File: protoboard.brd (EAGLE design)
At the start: 99.1 x 48.3 mm, 118 parts, among them J3 AVX_6-PIN_009159006061916, J4 CORTEX_DEBUG_PTH, J5 10118194-0001LF, U1 STM32F103C8T6, U2 CJT1117-3.3-SOT223

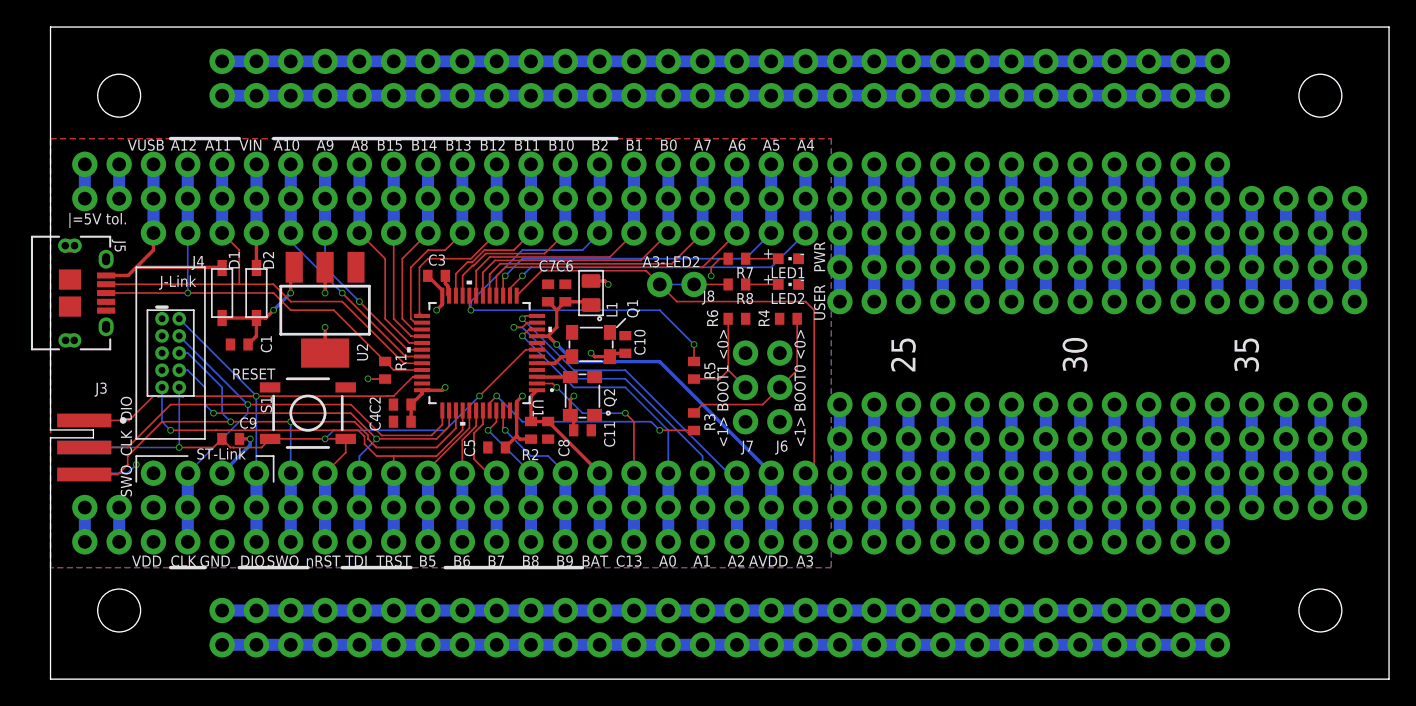
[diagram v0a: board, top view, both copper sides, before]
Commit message: Updated design block. Switched USB from micro-B to mini-B. Updated Debug Edge library.
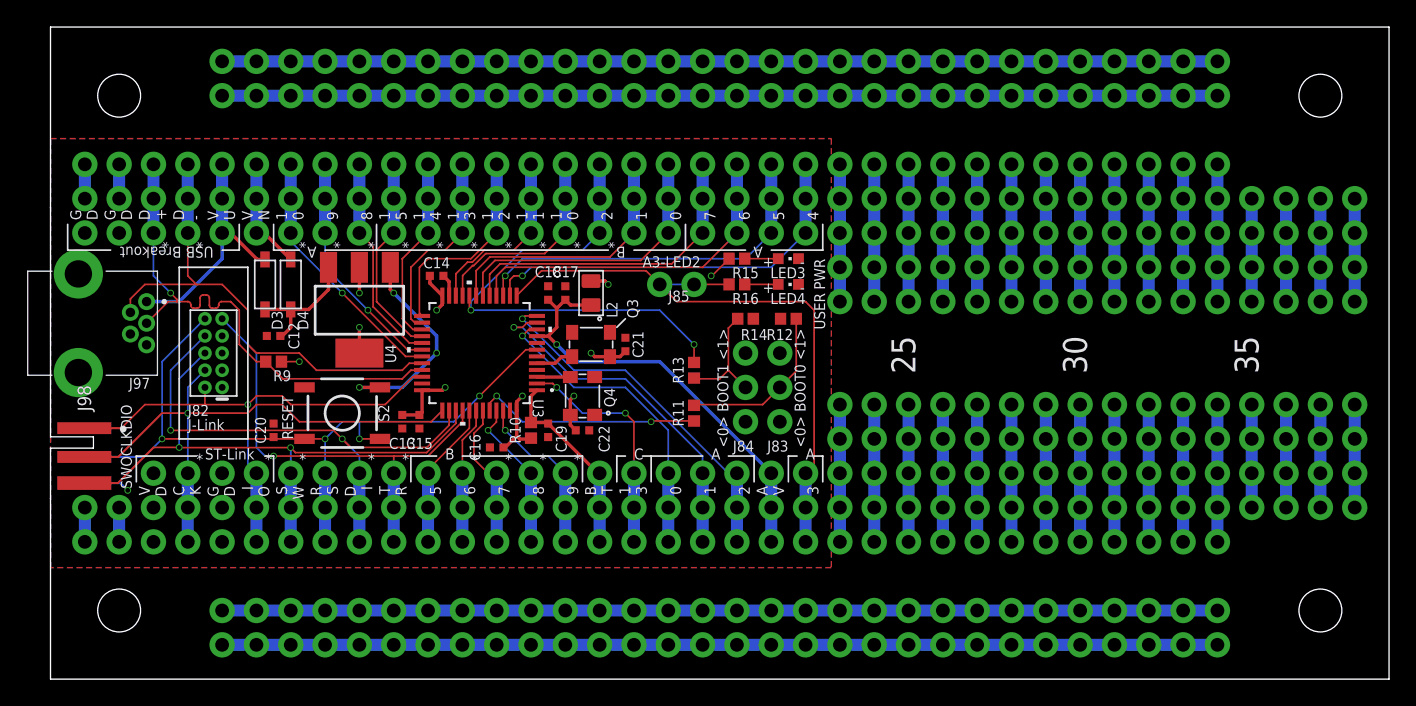
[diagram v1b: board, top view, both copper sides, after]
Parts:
- removed C1, C2: 10uF, adafruit:C0402
- removed C10, C11, C3, C4, C5, C7, C8, C9: 100nF, adafruit:C0402
- removed C6: 1uF, adafruit:C0402
- removed D1, D2: (no value), adafruit:SOD-123
- removed FRAME2: FRAME-LETTERNO_PACKAGE, SparkFun-Aesthetics:DUMMY
- removed J1: (no value), SparkFun-Connectors:1X20_NOSILK
- removed J3: AVX_6-PIN_009159006061916, Debug-Edge_AVX-connectors:AVX_6-PIN_009159006061916_0
- removed J4: CORTEX_DEBUG_PTH, SparkFun-Connectors:2X5-PTH-1.27MM
- removed J5: 10118194-0001LF, USB-micro-B_Amphenol_10118194-0001LF:CONN_10118194-0001LF_AMP
- removed R1: 1k5, adafruit:R0402
- removed R2, R4, R6: 0R, adafruit:R0402
- removed R3, R5: 10k, adafruit:R0402
- removed R7, R8: 150R, adafruit:R0402
- removed S1: MOMENTARY-SWITCH-SPST-SMD-5.2-REDUNDANT, SparkFun-Switches:TACTILE_SWITCH_SMD_5.2MM
- removed U2: CJT1117-3.3-SOT223, OPL_IC:SOT-223
- added C12, C13: 10uF, SparkFun-Capacitors:0402-TIGHT
- added C14, C15, C16, C18, C19, C20, C21, C22: 100nF, SparkFun-Capacitors:0402-TIGHT
- added C17: 1uF, SparkFun-Capacitors:0402-TIGHT
- added D3, D4: (no value), adafruit:SOD-123
- added FRAME1: FRAME-LETTERNO_PACKAGE, SparkFun-Aesthetics:DUMMY
- added J82: CORTEX_DEBUG_PTH, SparkFun-Connectors:2X5-PTH-1.27MM
- added J87, J88: (no value), SparkFun-Connectors:1X11_NO_SILK
- added J97: 2172034-1, 2172034-1:21720341
- added J98: AVX_6-PIN_009159006061916_33MIL-GAP, Debug-Edge_AVX-connectors:AVX_6-PIN_009159006061916_33MIL-GAP
- added R10, R12, R14: 0R, SparkFun-Resistors:0402
- added R11, R13: 10k, SparkFun-Resistors:0402
- added R15, R16: 150R, SparkFun-Resistors:0402
- added R9: 1k5, SparkFun-Resistors:0402
- added S2: MOMENTARY-SWITCH-SPST-SMD-5.2-REDUNDANT, SparkFun-Switches:TACTILE_SWITCH_SMD_5.2MM
- added U4: CJT1117-3.3-SOT223, OPL_IC:SOT-223
- renumbered J2 to J86, J6 to J83, J7 to J84, J8 to J85, L1 to L2, LED1 to LED3, LED2 to LED4, Q1 to Q3, Q2 to Q4, U1 to U3
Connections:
- removed net N$21: J13.1, J13.2
- removed net N$24: J15.1, J15.2
- removed net N$81: J83.2, R3.1, R4.2
- removed net N$82: J84.2, R5.1, R6.2
- removed net N$83: LED4.A, R8.2
- removed net N$84: LED3.A, R7.1
- removed net VIN: C1.1, D1.C, D2.C, U2.3
- new net N$58: J83.2, R11.1, R12.2
- new net N$59: J84.2, R13.1, R14.2
- new net N$60: LED4.A, R16.1
- new net N$61: LED3.A, R15.1
- new net VIN2: C12.1, D3.C, D4.C, U4.3
- net AVDD: now also C17.1, C18.1; no longer C6.1, C7.1
- net BOOT0: now also R11.2; no longer R3.2
- net BOOT1*: now also J87.7, R13.2; no longer J1.7, R5.2
- net GND: now also C12.2, C13.2, C14.2, C15.2, C16.2, C17.2, C18.2, C19.2, C20.2, C21.2, C22.2, J13.1, J13.2, J15.1, J15.2, J82.3, J82.5, J88.10, J88.11, J97.4, J97.5, J97.MH1, J97.MH2, J98.6, R12.1, R14.1, S2.1, S2.2, U4.1; no longer C1.2, C10.2, C11.2, C2.2, C3.2, C4.2, C5.2, C6.2, C7.2, C8.2, C9.2, J3.6, J4.3, J4.5, J5.10, J5.11, J5.4, J5.5, J5.S_1, J5.S_1_H1, J5.S_1_H2, J5.S_2, J5.S_2_H1, J5.S_2_H2, J5.S_3, J5.S_3_H1, J5.S_3_H2, J5.S_4, J5.S_4_H1, J5.S_4_H2, R4.1, R6.1, S1.1, S1.2, U2.1
- net JTDI*: now also J82.8; no longer J4.8
- net JTRST*: now also J82.9; no longer J4.9
- net NRST: now also C20.1, J82.10, J98.5, S2.3, S2.4; no longer C9.1, J3.5, J4.10, S1.3, S1.4
- net PA10*: now also J88.5; no longer J1.16
- net PA3: now also R16.2; no longer R8.1
- net PA4: now also J87.1; no longer J1.1
- net PA5: now also J87.2; no longer J1.2
- net PA6: now also J87.3; no longer J1.3
- net PA7: now also J87.4; no longer J1.4
- net PA8*: now also J88.3; no longer J1.14
- net PA9*: now also J88.4; no longer J1.15
- net PB0: now also J87.5; no longer J1.5
- net PB1: now also J87.6; no longer J1.6
- net PB10*: now also J87.8; no longer J1.8
- net PB11*: now also J87.9; no longer J1.9
- net PB12*: now also J87.10; no longer J1.10
- net PB13*: now also J87.11; no longer J1.11
- net PB14*: now also J88.1; no longer J1.12
- net PB15*: now also J88.2; no longer J1.13
- net SWCLK*: now also J82.4, J98.2; no longer J3.2, J4.4
- net SWDIO*: now also J82.2, J98.1; no longer J3.1, J4.2
- net SWO*: now also J82.6, J98.3; no longer J3.3, J4.6
- net USB_DM*: now also J19.1, J19.2, J88.8, J97.2; no longer J1.18, J45.1, J45.2, J5.2
- net USB_DP*: now also J17.1, J17.2, J88.9, J97.3, R9.1; no longer J1.19, J19.1, J19.2, J5.3, R1.1
- net VBAT_1.8-3.6V: now also C19.1, R10.1; no longer C8.1, R2.1
- net VDD: now also C13.1, C14.1, C15.1, C16.1, C21.1, C22.1, J82.1, J98.4, R10.2, R15.2, R9.2, U4.2, U4.TER; no longer C10.1, C11.1, C2.1, C3.1, C4.1, C5.1, J3.4, J4.1, R1.2, R2.2, R7.2, U2.2, U2.TER
- net VIN_4.8-15V: now also D4.A, J88.6; no longer D2.A, J1.17
- net VUSB: now also D3.A, J45.1, J45.2, J88.7, J97.1; no longer D1.A, J1.20, J17.1, J17.2, J5.1
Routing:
- net GND: track 9.93 -> 26.2 mm, vias 2 -> 4
- net N$81: track 12.7 -> 0.00 mm
- net N$58: track 0.00 -> 12.5 mm
- net VIN: track 10.1 -> 0.00 mm, vias 2 -> 0
- net VIN2: track 0.00 -> 9.33 mm
- net N$59: track 0.00 -> 8.72 mm
- net N$82: track 8.42 -> 0.00 mm
- net SWCLK*: track 49.3 -> 42.2 mm
- net JTDI*: track 32.5 -> 39.1 mm
- net SWDIO*: track 45.3 -> 38.8 mm
- net NRST: track 51.2 -> 57.5 mm, vias 3 -> 4
- net SWO*: track 48.3 -> 45.3 mm
- net USB_DP*: track 35.3 -> 38.0 mm
- net N$24: track 2.54 -> 0.00 mm
- net N$21: track 2.54 -> 0.00 mm
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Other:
- outline, holes or cut-outs redrawn
- board text added: "*"
- board text added: "-------POWER------- VDD/AVDD: 2-3.6V. Must be 3.3V if C39- 097/C387- 415 are used for Q1/Q2. VUSB: 5V from USB (J5) VIN: 4.8-15V BAT: 1.8-3.6V. Short R2 if unused. ***WARNING***: Do NOT power MCU from VDD if EITHER VIN or USB (J5) are also being used. --------GPIO-------- Max current, ea pin: 25 mA Max current, total: 150 mA OUT (minus MCU power, ~7 -50 mA) and 150 mA IN (minus MCU power) *=5V to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"
- board text added: "0"
- board text added: "1"
- board text added: "1 0"
- board text added: "1 1"
- board text added: "1 2"
- board text added: "1 3"
- board text added: "1 4"
- board text added: "1 5"
- board text added: "2"
- board text added: "3"
- board text added: "4"
- board text added: "5"
- board text added: "6"
- board text added: "7"
- board text added: "8"
- board text added: "9"
- board text added: "<0> BOOT0 <1>"
- board text added: "<0> BOOT1 <1>"
- board text added: "A"
- board text added: "A V"
- board text added: "B"
- board text added: "B T"
- board text added: "C"
- board text added: "C K"
- board text added: "D +"
- board text added: "D -"
- board text added: "D I"
- board text added: "FMI: github.com/nathancharlesjones/STM32F103C8T6-breakout-board"
- board text added: "G D"
- board text added: "GD"
- board text added: "I O"
- board text added: "R S"
- board text added: "S W"
- board text added: "T R"
- board text added: "USB Breakout"
- board text added: "V D"
- board text added: "V N"
- board text added: "V U"
- board text removed: "-------POWER------- VDD/AVDD: 2-3.6V. Must be 3.3V if C39- 097/C387- 415 are used for Q1/Q2. VUSB: 5V from USB (J5) VIN: 4.8-15V BAT: 1.8-3.6V. Short R2 if unused. ***WARNING***: Do NOT power MCU from VDD if EITHER VIN or USB (J5) are also being used. --------GPIO-------- Max current, ea pin: 25 mA Max current, total: 150 mA OUT (minus MCU power, ~7 -50 mA) and 150 mA IN (minus MCU po- wer) Bar o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"
- board text removed: "<1> BOOT0 <0>"
- board text removed: "<1> BOOT1 <0>"
- board text removed: "A0"
- board text removed: "A1"
- board text removed: "A10"
- board text removed: "A11"
- board text removed: "A12"
- board text removed: "A2"
- board text removed: "A3"
- board text removed: "A4"
- board text removed: "A5"
- board text removed: "A6"
- board text removed: "A7"
- board text removed: "A8"
- board text removed: "A9"
- board text removed: "AVDD"
- board text removed: "B0"
- board text removed: "B1"
- board text removed: "B10"
- board text removed: "B11"
- board text removed: "B12"
- board text removed: "B13"
- board text removed: "B14"
- board text removed: "B15"
- board text removed: "B2"
- board text removed: "B5"
- board text removed: "B6"
- board text removed: "B7"
- board text removed: "B8"
- board text removed: "B9"
- board text removed: "BAT"
- board text removed: "C13"
- board text removed: "GND"
- board text removed: "TDI"
- board text removed: "TRST"
- board text removed: "VIN"
- board text removed: "VUSB"
- board text removed: "|=5V tol."
